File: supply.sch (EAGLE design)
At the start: 8 parts, among them X1 ~24V

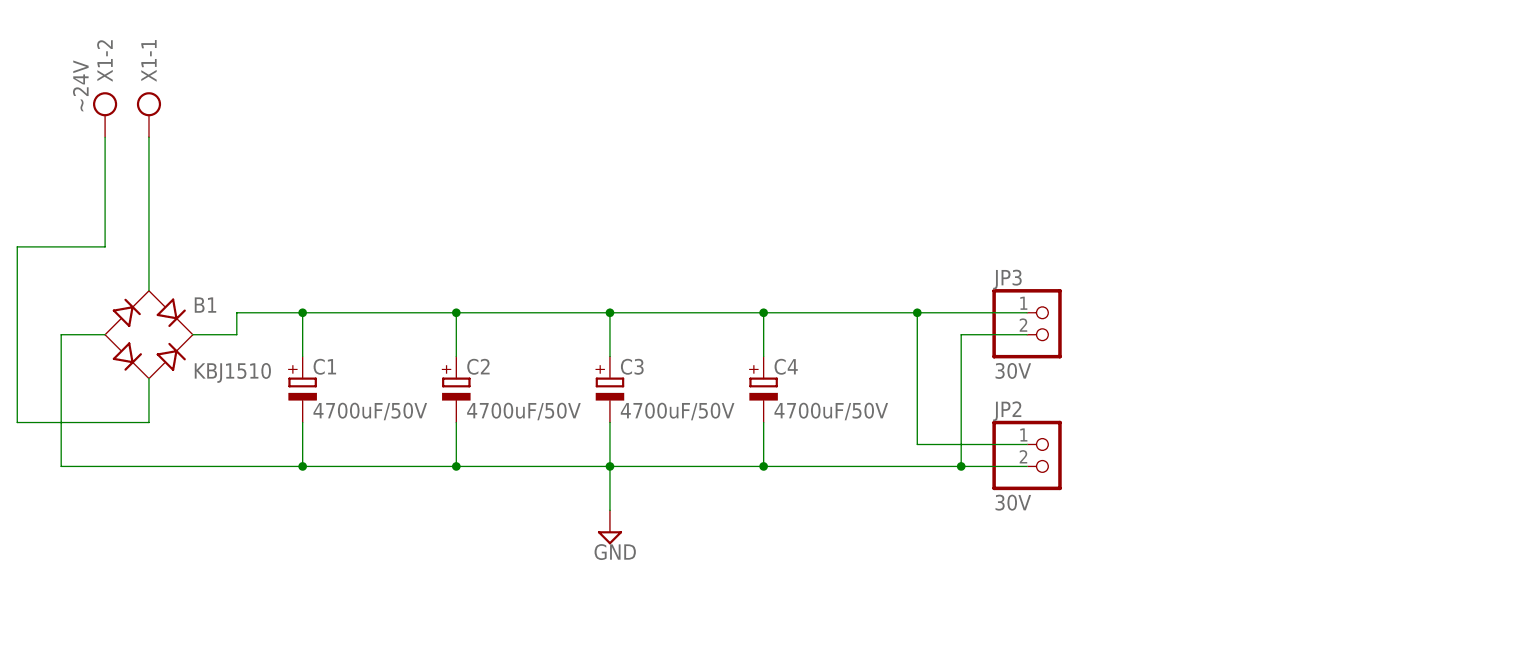
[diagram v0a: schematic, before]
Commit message: added schematics and iron controller logic
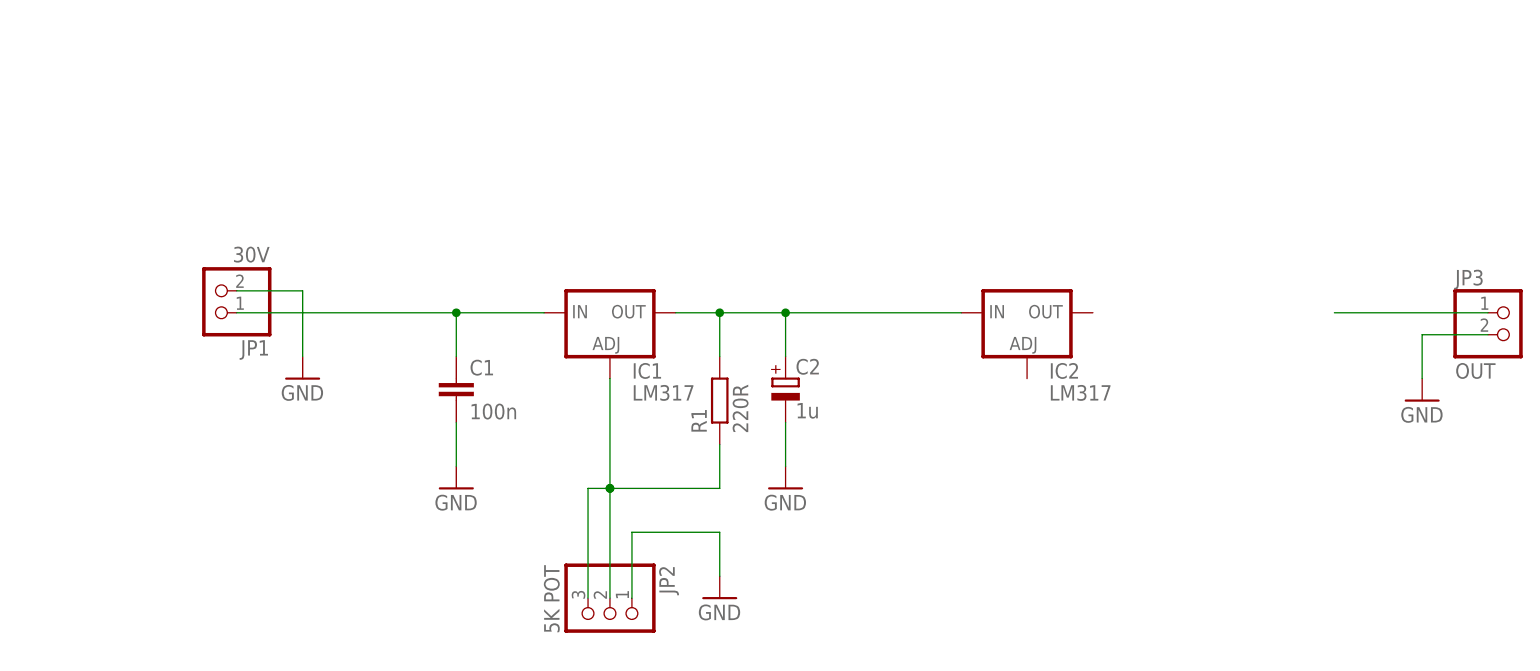
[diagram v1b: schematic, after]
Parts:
- removed B1: KBJ1510, rectifier:RECTIFIER-FB32
- removed C3, C4: 4700uF/50V, rcl:CPOL-EUE10-20
- removed X1: ~24V, con-ptr500:AK500/2
- added IC1, IC2: LM317, v-reg:LM317TS
- added JP1: 30V, pinhead:PINHD-1X2
- added R1: 220R, rcl:R-EU_0204/5
- C1: value 4700uF/50V -> 100n; device rcl:CPOL-EUE10-20 -> rcl:C-EU050-024X044
- C2: value 4700uF/50V -> 1u; device rcl:CPOL-EUE10-20 -> rcl:CPOL-EUE2-5
- JP2: value 30V -> 5K POT; device pinhead:PINHD-1X2 -> pinhead:PINHD-1X3
- JP3: value 30V -> OUT
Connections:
- removed net N$1: B1.AC2, X1-2.KL
- new net N$10: JP3.1
- new net N$4: IC1.ADJ, JP2.2, JP2.3, R1.1
- net GND: now also C1.2, JP1.2, JP2.1; no longer B1.-, C1.-, C3.-, C4.-, JP2.2
- net N$2: now also C1.1, IC1.IN, JP1.1; no longer B1.AC1, X1-1.KL
- net N$3: now also IC1.OUT, IC2.IN, R1.2; no longer B1.+, C1.+, C3.+, C4.+, JP2.1, JP3.1
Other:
- moved on the sheet: C2, JP3
